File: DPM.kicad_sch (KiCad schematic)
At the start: 26 parts, among them J1 Conn_02x12_Odd_Even, U1 74LS251, U25 74LS85, U28 74LS85, U3 ADG333A, U31 74LS85, U4 MCP23017_SP, U5 ADG333A, U6 ADG333A, U8 4040, U9 4040

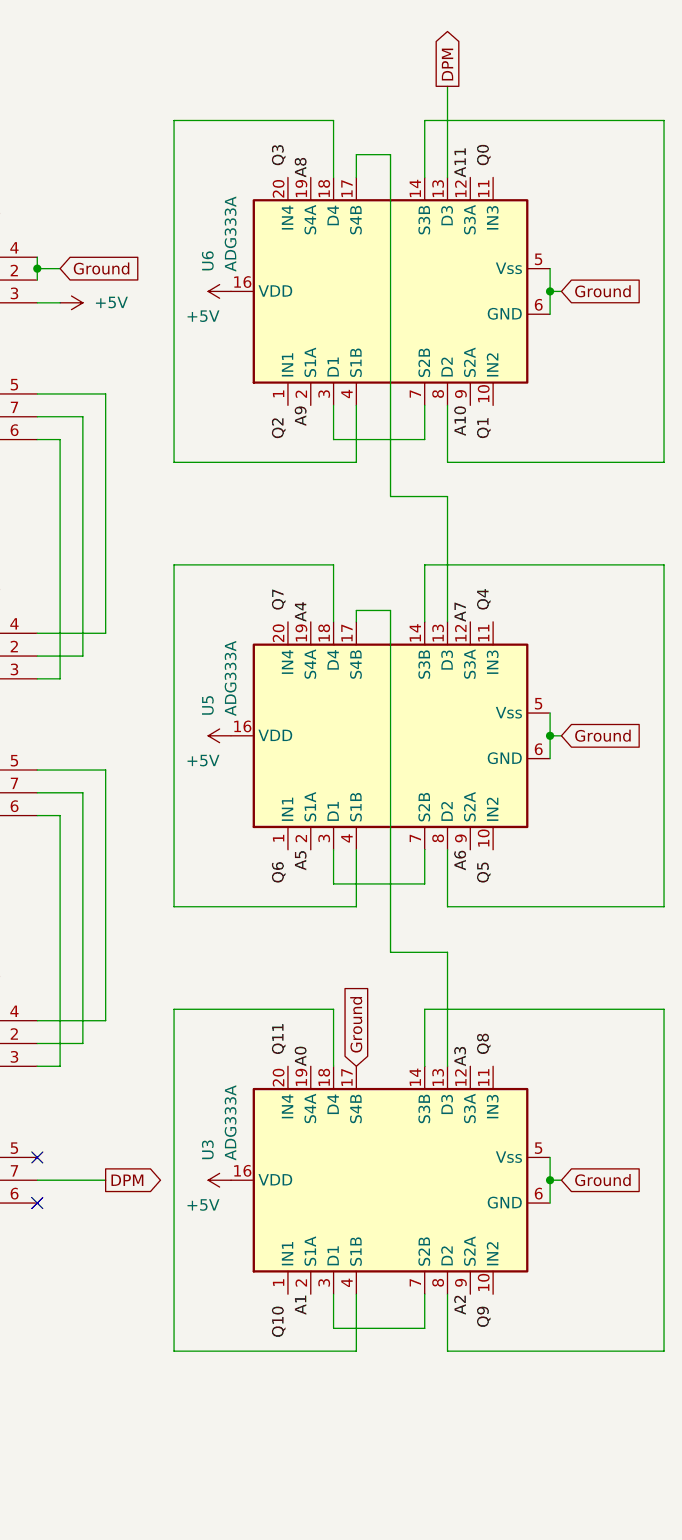
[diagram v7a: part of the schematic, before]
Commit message: Début de ré&vision pour ajouter des câblages
git-svn-id: file:///D%5C00%20-%20Dev%20&%20Calculs%5CRepoTortoiseSVN_PCB%5CD-DPM/trunk@19 f29d8339-a183-0348-962e-9e4594cf8312
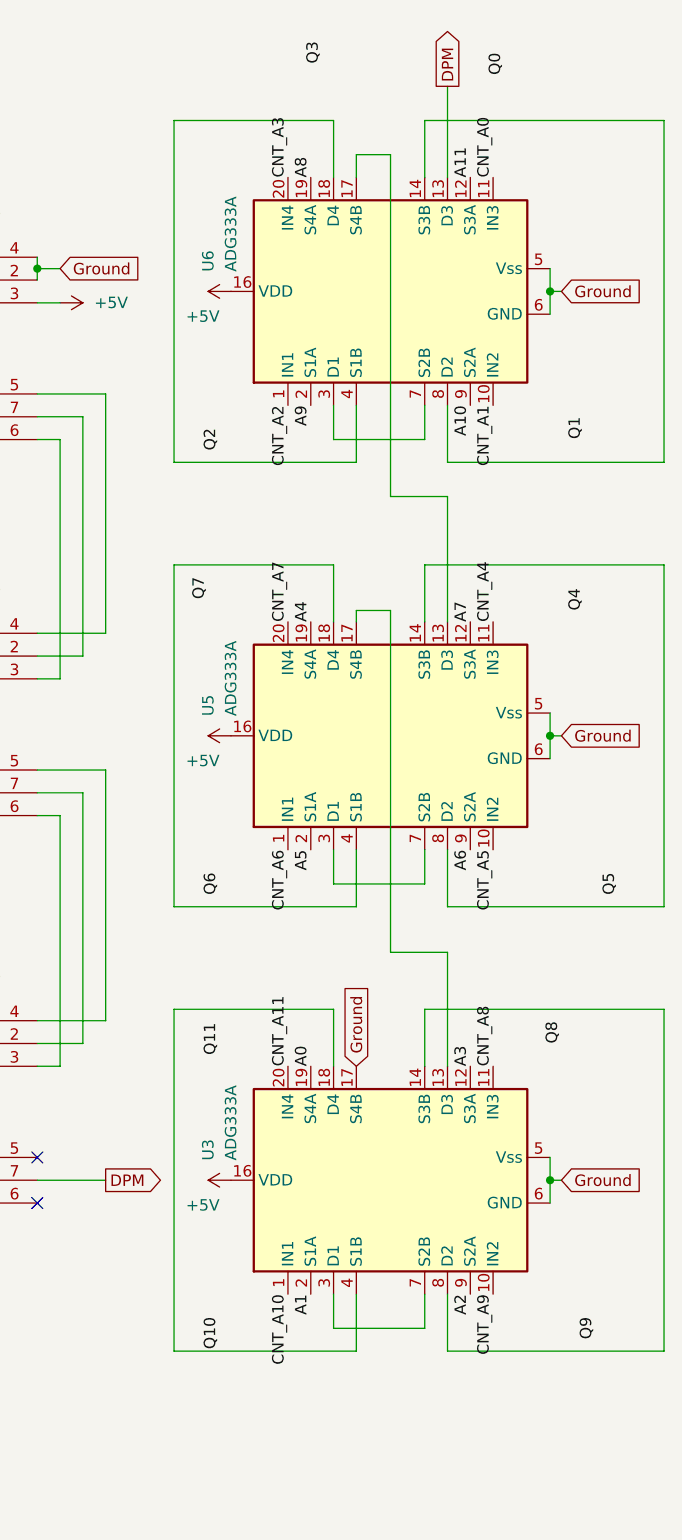
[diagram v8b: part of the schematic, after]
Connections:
- net CNT_A0: now also U6.11 (IN3)
- net CNT_A1: now also U6.10 (IN2)
- net CNT_A10: now also U3.1 (IN1)
- net CNT_A11: now also U3.20 (IN4)
- net CNT_A2: now also U6.1 (IN1)
- net CNT_A3: now also U6.20 (IN4)
- net CNT_A4: now also U5.11 (IN3)
- net CNT_A5: now also U5.10 (IN2)
- net CNT_A6: now also U5.1 (IN1)
- net CNT_A7: now also U5.20 (IN4)
- net CNT_A8: now also U3.11 (IN3)
- net CNT_A9: now also U3.10 (IN2)
